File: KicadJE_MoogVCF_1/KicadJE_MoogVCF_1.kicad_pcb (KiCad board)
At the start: 2 copper layers, 100 x 100 mm, 246 parts, among them J201 CV2, J202 Input2, J203 CV1, J204 Out VCF, J205 Input1, J301 ADSRGate, J302 ADSR, J401 CV, J402 Output, J403 VCA Out, J404 Input, P201 Doepfer_Power_10pin, P301 Doepfer_Power_10pin, P401 Doepfer_Power_10pin, Q201 UMX1N, Q202 SS9014, Q203 SS9014, Q204 SS9014, Q205 SS9014, Q206 SS9014, Q207 SS9014, Q208 UMX1N, Q209 UMX1N, Q210 UMX1N, Q211 SS9014, Q212 SS9015, Q301 SI2302, Q302 MMBT3904, Q303 MMBT3904, Q304 MMBT3904, Q401 UMX1N, Q402 SS9014, SW301 SW_DPDT_x2, SW302 Gate, SW401 Gate, U201 TL072, U301 TL072, U302 TLC555, U401 TL072, U402 TL074

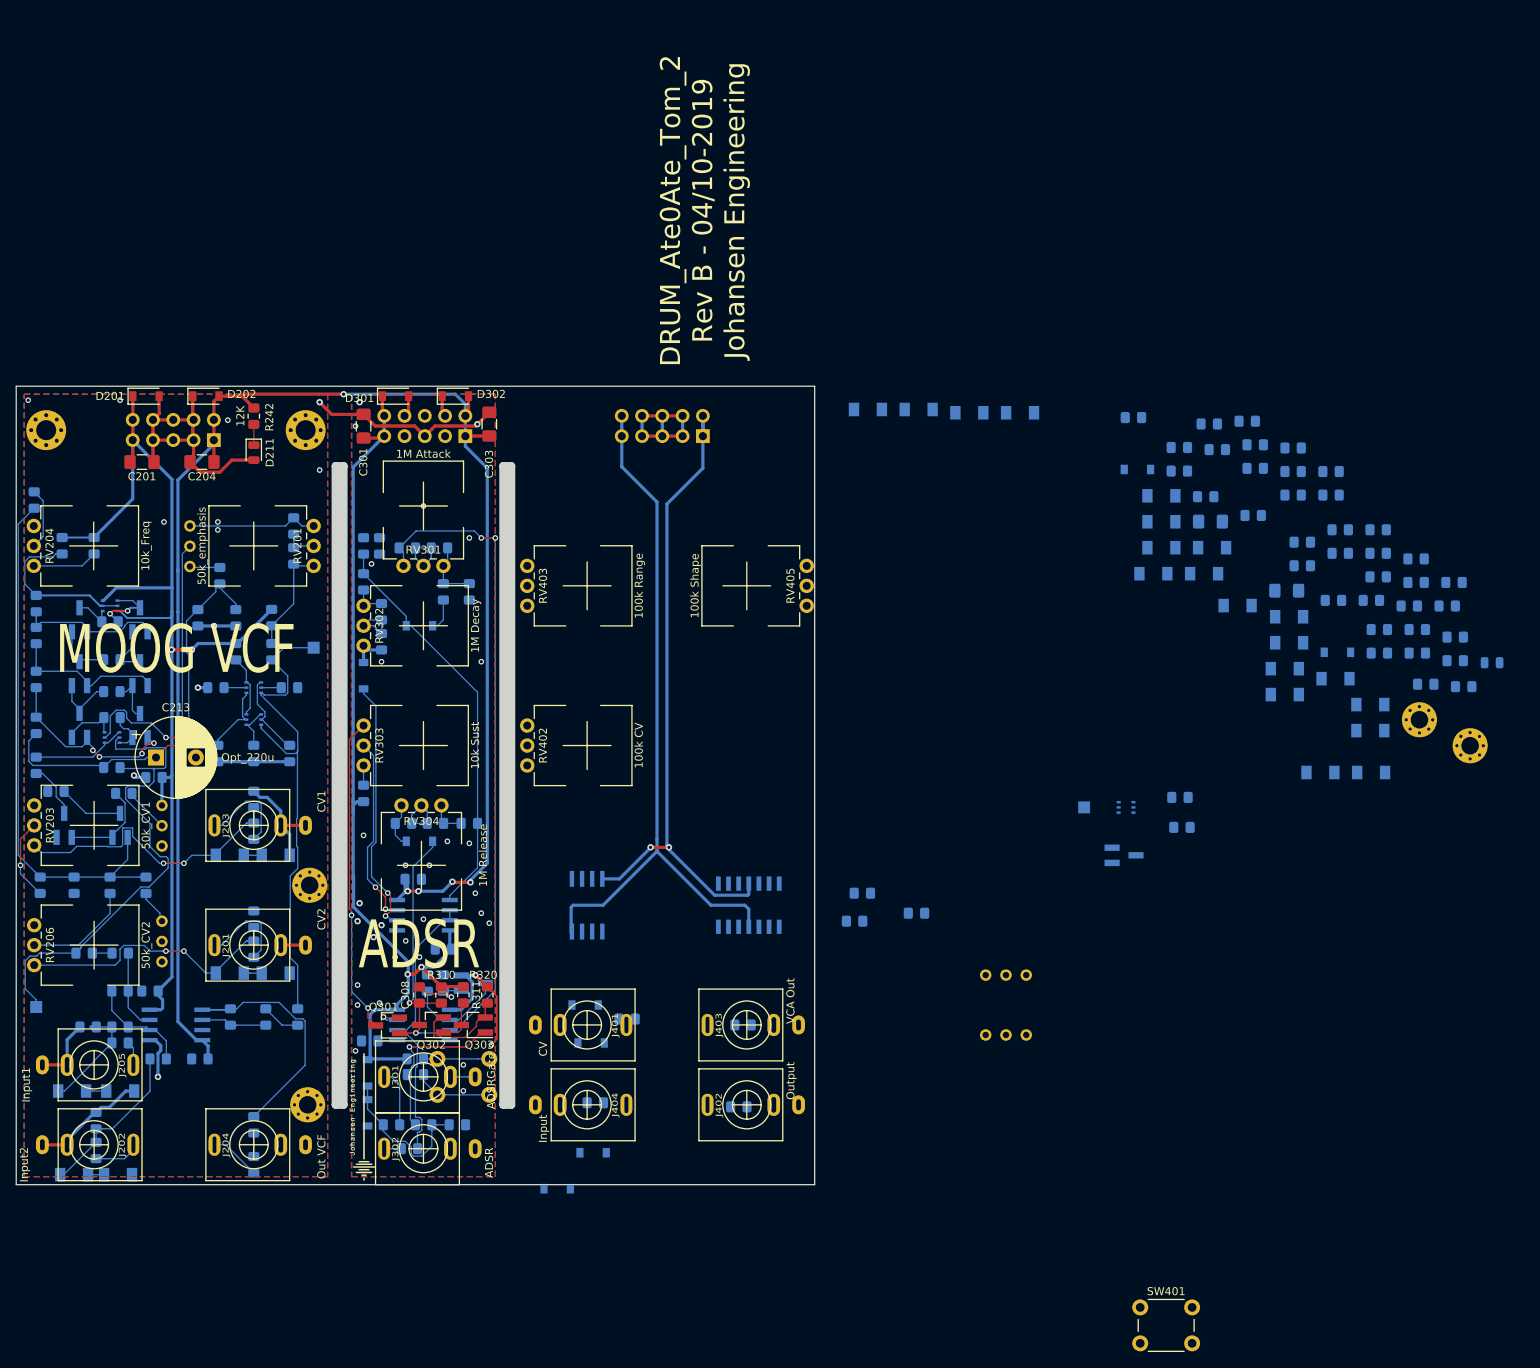
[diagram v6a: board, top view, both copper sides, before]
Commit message: Routed Wavefolder
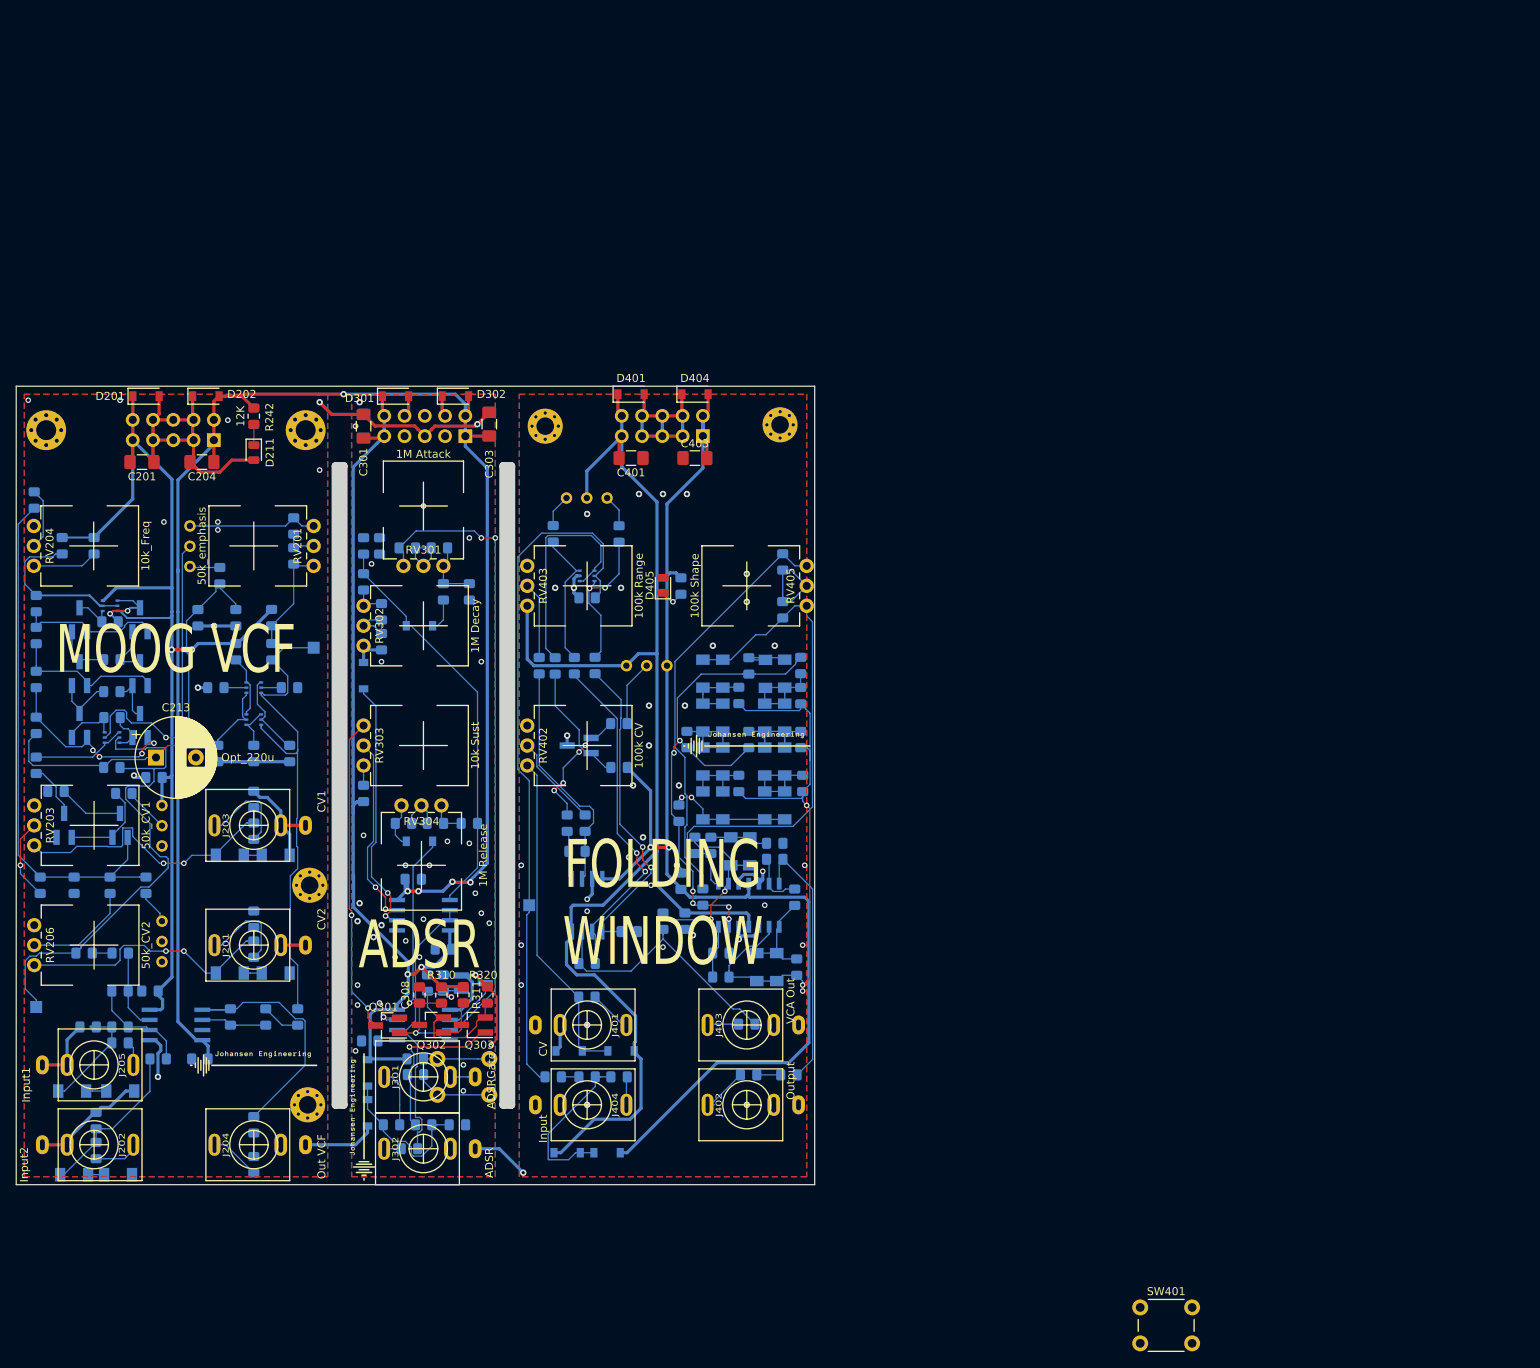
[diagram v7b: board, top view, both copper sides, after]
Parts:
- added G***: LOGO, AJ:Johansen_engineering_logo_20mm, F.Cu at (79.8, 135.0)
- added G***: LOGO, AJ:Johansen_engineering_logo_20mm, F.Cu at (141.5, 95.0)
- C401, C403, D401, D404, D405: moved to F.Cu
- U402: footprint AJ:SOIC-14_3.9x8.7mm_P1.27mm -> Package_SO:SOIC-14_3.9x8.7mm_P1.27mm
- moved H402 122.6 mm to (116.2, 55.0)
- moved R412 116.7 mm to (121.5, 136.5)
- moved R420 113.8 mm to (117.5, 85.0), turned to 90 degrees
- moved R407 112.3 mm to (117.2, 68.5), turned to 90 degrees
- moved R409 110.7 mm to (121.5, 122.3)
- moved R440 104.7 mm to (131.0, 117.0), turned to 270 degrees
- moved D405 104.3 mm to (131.0, 74.9), turned to 90 degrees
- moved R406 102.9 mm to (138.2, 121.0), turned to 180 degrees
- moved R410 95.4 mm to (119.9, 85.0), turned to 90 degrees
- moved D401 94.2 mm to (127.0, 51.0)
- moved R422 93.0 mm to (115.5, 85.0), turned to 270 degrees
- moved R437 92.5 mm to (137.0, 107.5), turned to 90 degrees
- moved R415 91.8 mm to (126.8, 118.3), turned to 180 degrees
- moved R428 91.1 mm to (136.0, 114.0), turned to 270 degrees
- moved R425 91.1 mm to (125.5, 97.8), turned to 180 degrees
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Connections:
- D410 pad 1: Net-(D410-Pad1) -> Net-(C407-Pad2)
- D411 pad 2: Net-(D410-Pad1) -> Net-(C407-Pad2)
- D418 pad 1: Net-(D418-Pad1) -> Net-(D414-Pad1)
- D419 pad 2: Net-(D418-Pad1) -> Net-(D414-Pad1)
- D424 pad 1: Net-(D424-Pad1) -> Net-(D420-Pad1)
- D425 pad 2: Net-(D424-Pad1) -> Net-(D420-Pad1)
- R429 pad 1: Net-(D418-Pad1) -> Net-(D414-Pad1)
- R434 pad 1: Net-(D424-Pad1) -> Net-(D420-Pad1)
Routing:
- net Net-(C405-Pad1): track 0.00 -> 87.4 mm
- net +12V: track 347.0 -> 429.2 mm
- net Net-(C407-Pad1): track 0.00 -> 76.8 mm, vias 0 -> 2
- net -12V: track 302.2 -> 378.7 mm
- net Net-(D426-Pad1): track 0.00 -> 67.7 mm
- net Net-(C406-Pad2): track 0.00 -> 66.7 mm, vias 0 -> 6
- net Net-(R428-Pad1): track 0.00 -> 52.9 mm
- net GND: track 155.9 -> 203.5 mm, vias 44 -> 82
- net Net-(R409-Pad2): track 0.00 -> 43.1 mm, vias 0 -> 2
- net CV_Fold: track 0.00 -> 41.8 mm
- net Net-(R413-Pad1): track 0.00 -> 40.3 mm, vias 0 -> 2
- net Output_VCA: track 0.00 -> 33.9 mm
- net Net-(C408-Pad1): track 0.00 -> 32.6 mm
- net Net-(R417-Pad1): track 0.00 -> 29.8 mm
- net Net-(Q401-Pad1): track 0.00 -> 28.9 mm
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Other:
- board text added: "FOLDING WINDOW"
- board text added: "KicadJE_WaveFolder Rev A - 07/10-2019 Johansen Engineering"
- board text removed: "DRUM_Ate0Ate_Tom_1 Rev B - 04/10-2019 Johansen Engineering"
- board text removed: "DRUM_Ate0Ate_Tom_2 Rev B - 04/10-2019 Johansen Engineering"

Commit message: Wavefolder labeled
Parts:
- removed G*** (x2): LOGO, AJ:Johansen_engineering_logo_20mm
- R401, R405: value 47k -> 10k
